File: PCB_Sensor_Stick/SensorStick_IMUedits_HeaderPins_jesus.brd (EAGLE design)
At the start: 63.5 x 38.1 mm, 32 parts, among them IC1 SAM-M8Q-0-10, IC2 STM32L412RBT6P, IC3 DPS310XTSA1, IC5 BMI085, IC6 IIS2MDCTR, J1 USB4160-03-0230-C, U1 4525DO-DS5AI001DP, U2 LD39050PU33R

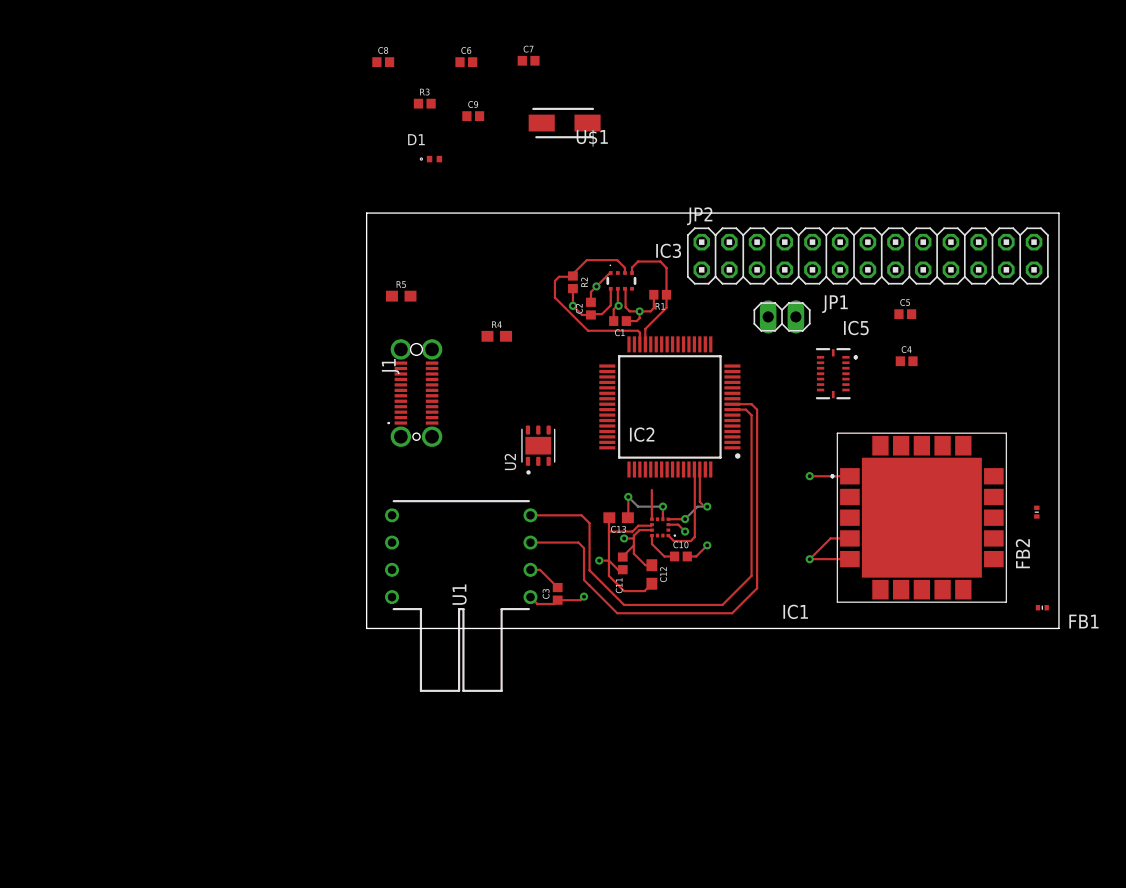
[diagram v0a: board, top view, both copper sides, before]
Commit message: J - Current PCB layout, USB-C and power needed
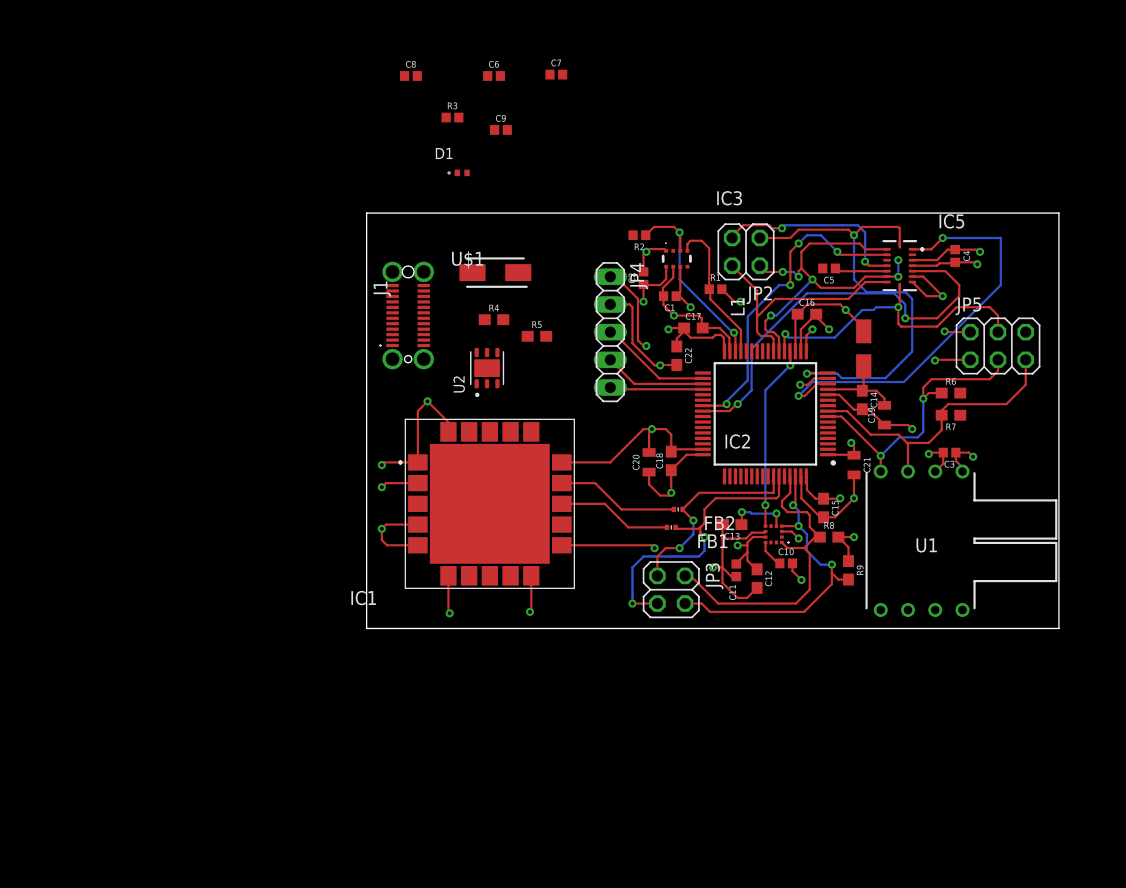
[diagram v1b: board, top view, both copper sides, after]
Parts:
- removed JP1: (no value), pinhead:1X02
- added C14, C15, C16, C17, C18: 0.1uF, SparkFun-Capacitors:0603
- added C19, C20, C21: 1.0uF, SparkFun-Capacitors:0805
- added C22: 4.7uF, SparkFun-Capacitors:0603
- added JP3: (no value), pinhead:2X02
- added JP4: (no value), pinhead:1X05
- added JP5: (no value), pinhead:2X03
- added L1: (no value), rcl:L4035M
- added R6, R7, R8, R9: 4.7k, SparkFun-Resistors:0603
- JP2: device pinhead:2X13 -> pinhead:2X02
- moved U1 49.2 mm to (55.8, 6.10), turned to 180 degrees
- moved IC1 39.6 mm to (11.3, 11.4)
- moved C3 38.2 mm to (53.5, 16.1), turned to 180 degrees
- moved FB1 34.8 mm to (27.9, 9.27)
- moved FB2 32.9 mm to (28.6, 10.9), turned to 0 degrees
- moved U$1 15.1 mm to (11.8, 32.6), turned to 180 degrees
- moved R5 13.0 mm to (15.6, 26.8)
- moved IC5 11.6 mm to (48.9, 33.3)
- moved JP2 11.2 mm to (34.8, 34.5), turned to 180 degrees
- moved C4 10.6 mm to (54.0, 34.2), turned to 270 degrees
- moved IC6 10.4 mm to (37.3, 8.64)
- moved C11 10.4 mm to (33.9, 5.33)
- moved C13 10.4 mm to (33.5, 9.53)
- moved C10 9.67 mm to (38.5, 5.97)
- moved C12 9.66 mm to (35.8, 4.57)
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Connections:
- removed net N$14: JP2.6
- removed net N$29: JP2.16
- removed net N$30: JP2.18
- removed net N$31: JP2.20
- removed net N$9: IC5.16, JP1.1
- removed net USB_DM: IC2.44
- new net INT_3: IC5.12, JP2.3
- new net N$11: JP5.6
- new net VREF: C14.1, C19.2, IC2.13, L1.1
- net 3V3: now also C15.1, C16.1, C17.1, C18.1, C20.1, C21.1, C22.1, IC2.19, IC2.32, IC2.48, IC2.64, JP4.1, JP5.1, L1.2, R8.2, R9.1; no longer JP2.24
- net 5V: now also R6.2, R7.1; no longer JP2.22
- net GND: now also C14.2, C15.2, C16.2, C17.2, C18.2, C19.1, C20.2, C21.2, C22.2, IC2.12, IC2.18, IC2.31, IC2.47, IC2.63, JP4.2, JP5.2; no longer JP2.25, JP2.26
- net GPIO_EXTI0: no longer JP2.8
- net GPIO_EXTI1: no longer JP2.10
- net GPIO_EXTI2: now also IC5.16, JP2.1; no longer IC5.12, JP1.2, JP2.12
- net GPIO_EXTI4: no longer JP2.14
- net I2C1_SCL: now also JP3.2, R8.1; no longer JP2.3
- net I2C1_SDA: now also JP3.4, R9.2; no longer JP2.1
- net I2C2_SCL: no longer JP2.7
- net I2C2_SDA: no longer JP2.5
- net I2C3_SCL: now also JP5.3, R6.1; no longer JP2.11
- net I2C3_SDA: now also JP5.5, R7.2; no longer JP2.9
- net SPI1_MISO: now also JP2.2; no longer JP2.15
- net SPI1_MOSI: now also JP2.4; no longer JP2.17
- net SPI1_SCK: now also JP5.4; no longer JP2.13
- net SPI2_MISO: now also JP4.4; no longer JP2.21
- net SPI2_MOSI: now also JP4.5; no longer JP2.23
- net SPI2_SCK: now also JP4.3; no longer JP2.19
- net USART1_RX: now also JP3.3
- net USART1_TX: now also JP3.1
- net USART3_RX: no longer JP2.2
- net USART3_TX: no longer JP2.4
- net USB_DN: now also IC2.44
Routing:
- net GND: track 44.8 -> 146.5 mm, vias 8 -> 20
- net 3V3: track 26.2 -> 90.4 mm, vias 3 -> 15
- net GPIO_EXTI2: track 0.00 -> 43.0 mm, vias 0 -> 2
- net GPIO_EXTI0: track 0.00 -> 38.8 mm, vias 0 -> 2
- net CSB_GYRO: track 0.00 -> 38.6 mm, vias 0 -> 2
- net SPI1_MISO: track 0.00 -> 35.8 mm, vias 0 -> 6
- net CSB_ACCEL: track 0.00 -> 29.5 mm, vias 0 -> 4
- net SPI1_SCK: track 0.00 -> 28.6 mm, vias 0 -> 2
- net USART1_RX: track 0.00 -> 28.5 mm, vias 0 -> 2
- net SPI1_MOSI: track 0.00 -> 23.2 mm
- net I2C1_SDA: track 7.88 -> 30.2 mm, vias 2 -> 3
- net I2C1_SCL: track 9.00 -> 29.5 mm
- net USART1_TX: track 0.00 -> 19.1 mm, vias 0 -> 2
- net INT_3: track 0.00 -> 18.1 mm, vias 0 -> 2
- net I2C3_SDA: track 45.0 -> 27.5 mm
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
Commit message: J- Added power supply module to layout, missing USB-C
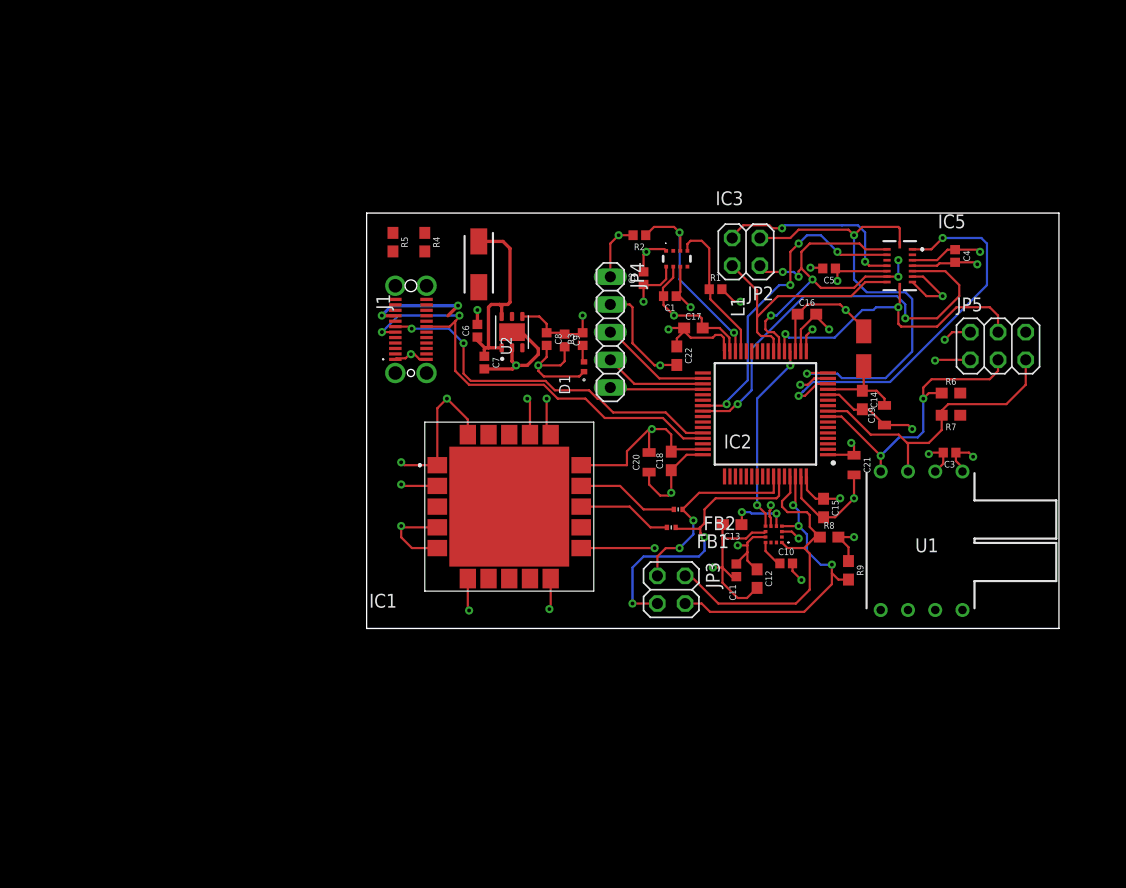
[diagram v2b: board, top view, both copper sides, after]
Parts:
- moved C7 27.2 mm to (10.8, 24.4), turned to 270 degrees
- moved C8 27.2 mm to (16.5, 26.5), turned to 270 degrees
- moved R3 23.6 mm to (19.8, 26.5), turned to 90 degrees
- moved C6 23.4 mm to (10.2, 27.3), turned to 90 degrees
- moved D1 21.0 mm to (19.9, 24.0), turned to 90 degrees
- moved C9 20.2 mm to (18.2, 26.4), turned to 270 degrees
- moved R5 15.8 mm to (2.41, 35.4), turned to 270 degrees
- moved R4 9.53 mm to (5.33, 35.4), turned to 270 degrees
- moved U2 4.02 mm to (13.3, 27.2)
- moved IC1 1.80 mm to (13.1, 11.2)
- moved U$1 1.70 mm to (10.3, 33.4), turned to 270 degrees
- moved J1 1.30 mm to (4.06, 27.4)
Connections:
- net 5V: no longer J1.A4, J1.A9, J1.B4, J1.B9
- net 5V_IN: now also J1.A4, J1.A9, J1.B4, J1.B9
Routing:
- net USB_DP: track 0.00 -> 42.3 mm, vias 0 -> 2
- net USB_DN: track 0.00 -> 33.9 mm, vias 0 -> 2
- net GND: track 146.5 -> 177.6 mm, vias 20 -> 27
- net 5V: track 0.00 -> 18.8 mm
- net 3V3: track 90.4 -> 100.5 mm, vias 15 -> 18
- net 5V_IN: track 0.00 -> 9.93 mm, vias 0 -> 2
- net GPIO_EXTI0: track 38.8 -> 35.9 mm
- net TX: track 10.5 -> 8.65 mm
- net N$2: track 11.3 -> 9.39 mm
- net N$5: track 0.00 -> 1.56 mm
- net GPIO_EXTI4: track 17.0 -> 17.7 mm
- added copper zone on layer 15, net 3V3
- removed copper zone on layer 15, net 3.3V

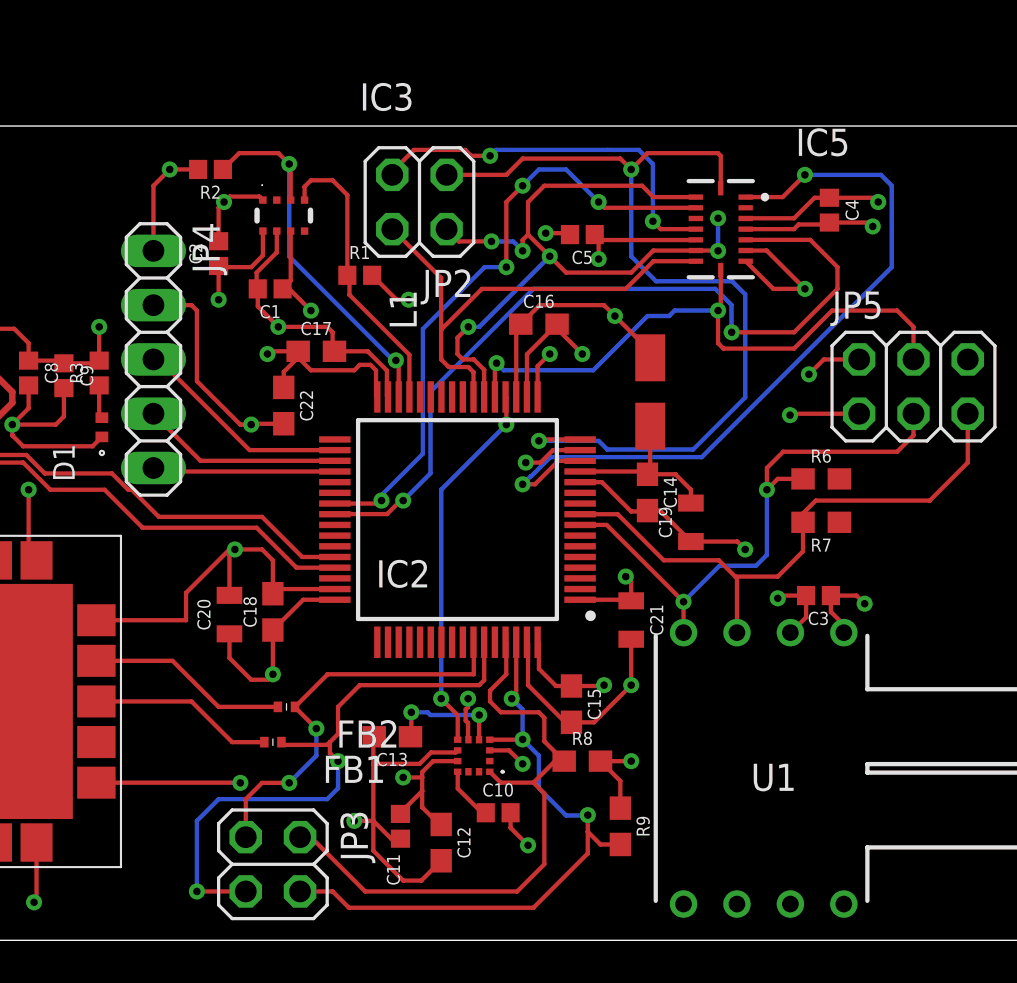
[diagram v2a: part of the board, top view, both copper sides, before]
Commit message: J- Edited data ready lines and connections, Barometer missing
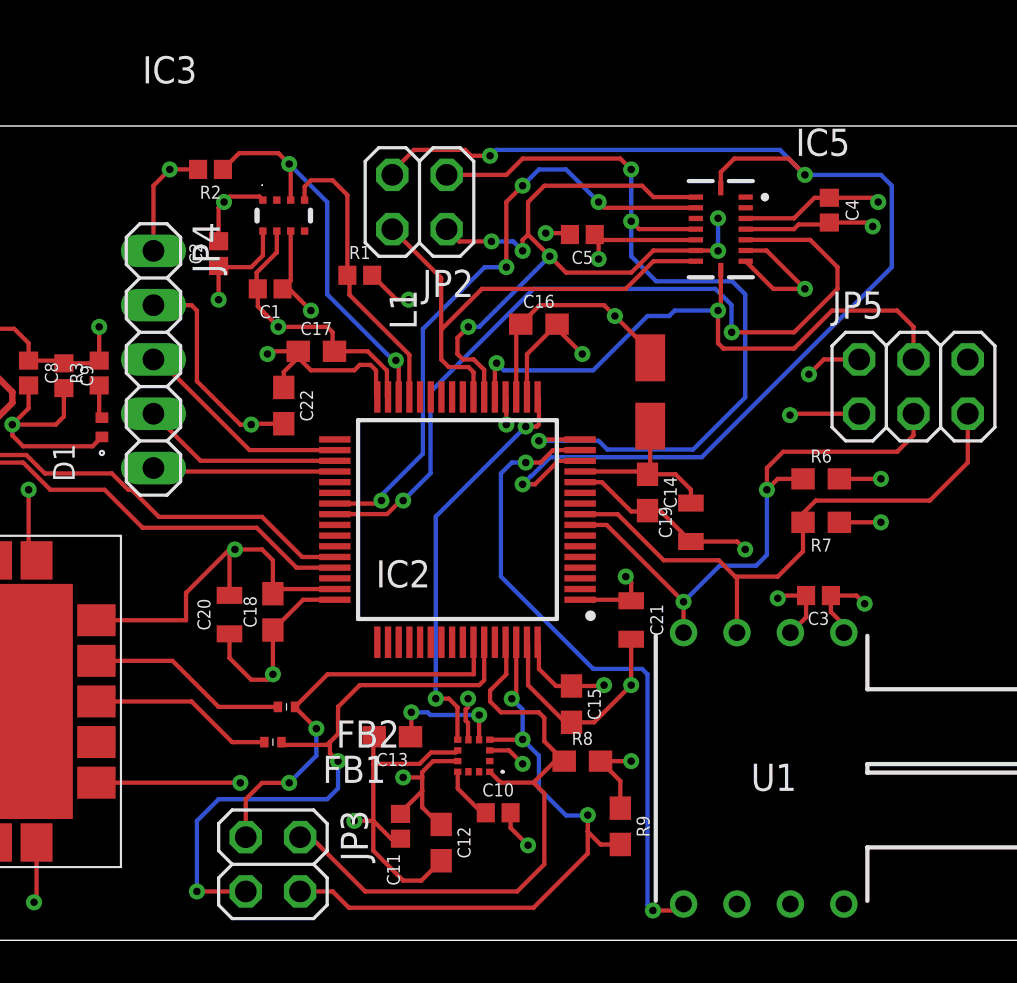
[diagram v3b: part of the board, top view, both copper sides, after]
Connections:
- removed net INT_3: IC5.12, JP2.3
- net 3V3: now also R6.2, R7.1
- net 5V: no longer R6.2, R7.1
- net GPIO_EXTI0: now also IC5.16, JP2.3; no longer IC5.1
- net GPIO_EXTI1: now also U1.5
- net GPIO_EXTI2: now also IC5.12; no longer IC5.16
- net GPIO_EXTI3: now also IC6.7
- net GPIO_EXTI4: no longer IC6.7
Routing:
- net GPIO_EXTI1: track 2.78 -> 30.5 mm, vias 1 -> 2
- net GPIO_EXTI0: track 35.9 -> 58.6 mm, vias 2 -> 3
- net INT_3: track 18.1 -> 0.00 mm, vias 2 -> 0
- net GPIO_EXTI3: track 2.24 -> 19.2 mm, vias 1 -> 2
- net GPIO_EXTI4: track 17.7 -> 1.31 mm, vias 2 -> 1
- net 3V3: track 100.5 -> 104.4 mm, vias 18 -> 20
- net GPIO_EXTI2: track 43.0 -> 40.1 mm, vias 2 -> 3

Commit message: J- Connected interrupt line for barometer
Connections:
- net GPIO_EXTI4: now also IC3.5
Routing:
- net GPIO_EXTI4: track 1.31 -> 25.7 mm, vias 1 -> 2
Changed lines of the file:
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@@
 <wire x1="38.862" y1="25.387" x2="38.862" y2="24.13" width="0.2032" layer="1"/>
 <via x="38.862" y="24.13" extent="1-16" drill="0.35"/>
+<contactref element="IC3" pad="5"/>
+<wire x1="38.862" y1="24.13" x2="33.528" y2="18.796" width="0.2032" layer="16"/>
+<wire x1="33.528" y1="18.796" x2="32.258" y2="18.796" width="0.2032" layer="16"/>
+<wire x1="32.258" y1="18.796" x2="31.75" y2="19.304" width="0.2032" layer="16"/>
+<wire x1="31.75" y1="28.448" x2="29.464" y2="30.734" width="0.2032" layer="16"/>
+<wire x1="29.464" y1="30.734" x2="29.464" y2="31.496" width="0.2032" layer="16"/>
+<via x="29.464" y="31.496" extent="1-16" drill="0.35"/>
+<wire x1="29.464" y1="31.496" x2="29.464" y2="33.143" width="0.2032" layer="1"/>
+<wire x1="29.464" y1="33.143" x2="29.423" y2="33.184" width="0.2032" layer="1"/>
+<wire x1="31.75" y1="19.304" x2="31.75" y2="28.448" width="0.2032" layer="16"/>
 </signal>
 <signal name="USART3_RX">

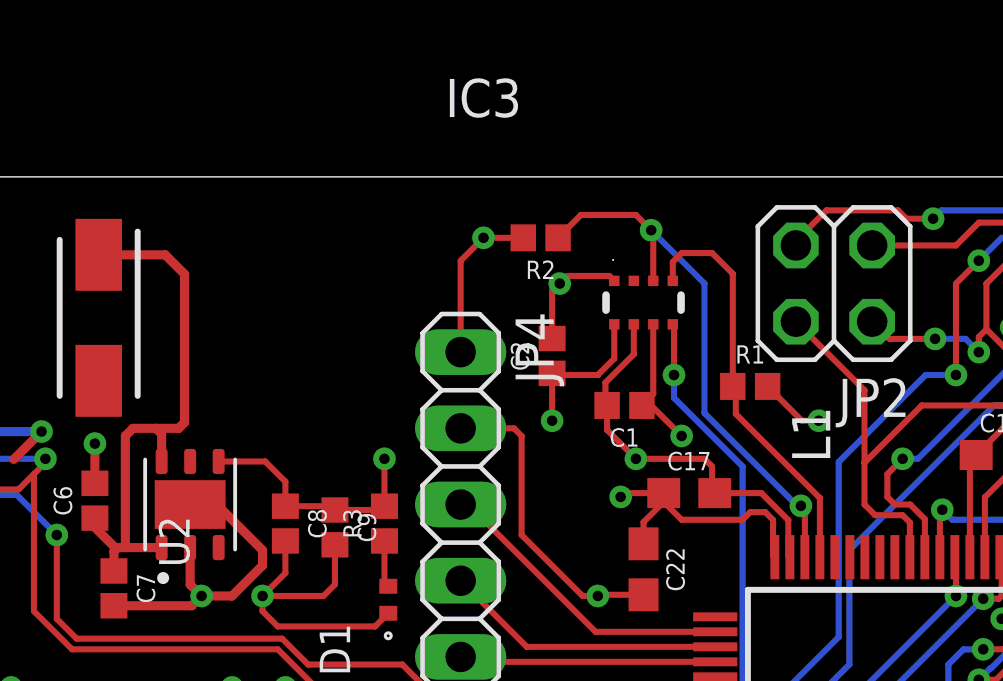
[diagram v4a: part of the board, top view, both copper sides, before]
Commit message: J - Added header pins for remaining I2C lines
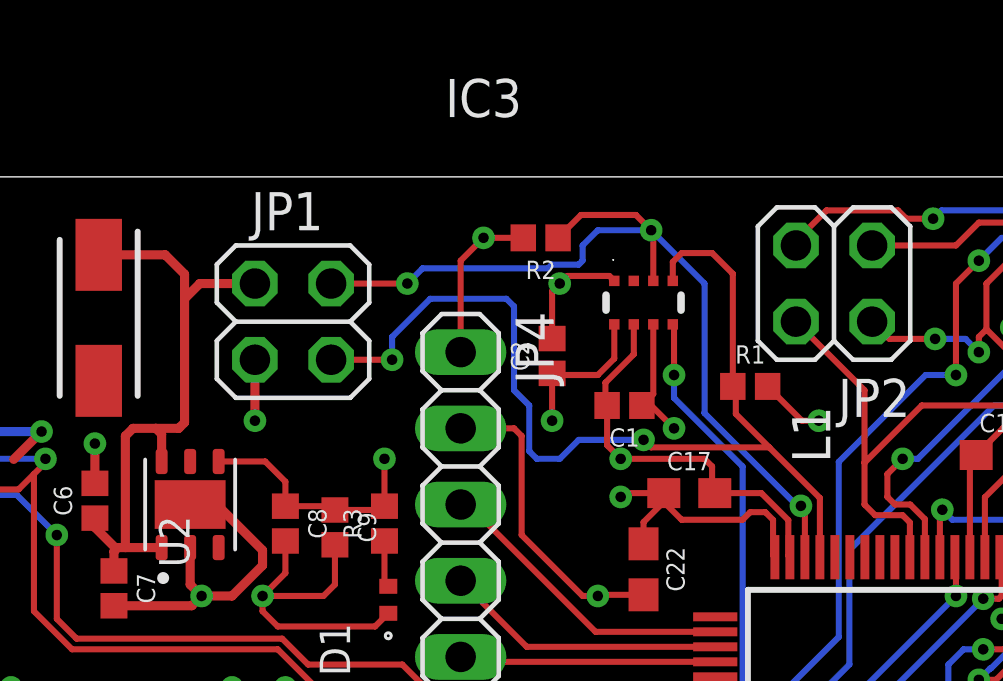
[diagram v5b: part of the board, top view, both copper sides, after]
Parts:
- added JP1: (no value), pinhead:2X02
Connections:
- net 5V: now also JP1.1
- net GND: now also JP1.3
- net I2C2_SCL: now also JP1.4
- net I2C2_SDA: now also JP1.2
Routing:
- net I2C2_SCL: track 13.8 -> 34.8 mm, vias 0 -> 2
- net I2C2_SDA: track 18.4 -> 30.1 mm, vias 2 -> 3
- net 5V: track 18.8 -> 21.3 mm
- net GND: track 177.6 -> 179.9 mm, vias 27 -> 28
